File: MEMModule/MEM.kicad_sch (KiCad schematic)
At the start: 5 parts, among them U1 74ABT32, U2 74AHCT04

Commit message: MEMModule now has ROM on Bank 0 again
The idea of having a system with no built-in ROM is turning out to be more
complicated than I expected. The boot device is additional complexity that
I'm now reluctant to take on. It's still, after months, not fully designed
and prototyped. Let's eliminate the need for this entire module by having
the computer run from ROM on boot.

The benefits of a ROM-less system are more difficult to achieve than
expected. The device would need a fast sixteen bit ALU chip as in the
program counter. Using simple counters like the 74F161 would bottleneck the
counting sopeed at 12.5MHz and the boot device provides no effective speed
benefit.

Further, the entire scheme is a performance optimization for a machine that
hasn't even been fully constructed yet. I can take on optimization work
later.

So this change sticks a pair of fast ROMS into MEM on Bank zero. A program
can set the Bank register to something else in order to map the built-in
RAM to instruction memory instead.

Also, update MEMModule for KiCad 7.
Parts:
- removed unit 4 of U2
- removed unit 3 of U2
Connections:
- no-connect marks 6 -> 4

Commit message: Update part info and data sheet links, move onto the 1.27mm grid
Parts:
- C2, C3: value 100nF -> 0.1μF
- U2: Mouser https://www.mouser.com/ProductDetail/771-AHCT04PW112 -> https://www.mouser.com/ProductDetail/Nexperia/74AHCT04APWJ?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

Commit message: MEMModule: Fix bug in the bank register reset signal
The bank register expects an active-high reset signal but was wired to
receive an active-low signal. Fix this issue by routing /RST_sync through
an inverter first.

BUG: The MainBoard PCB layout has not been updated yet.
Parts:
- removed unit 5 of U2
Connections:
- no-connect marks 4 -> 3
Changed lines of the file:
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@@
   (junction (at -44.45 146.05) (diameter 0) (color 0 0 0 0)
-  )
-  (junction (at -21.59 133.35) (diameter 0) (color 0 0 0 0)
   )
   (junction (at -44.45 130.81) (diameter 0) (color 0 0 0 0)
@@
   (no_connect (at -6.35 146.05))
   (no_connect (at -26.67 128.27))
-  (no_connect (at -6.35 133.35))
   (no_connect (at -26.67 143.51))
   (bus_entry (at 58.42 58.42) (size 2.54 2.54)
@@
     (stroke (width 0) (type default))
   )
-  (wire (pts (xy -21.59 97.79) (xy -21.59 133.35))
+  (wire (pts (xy -21.59 97.79) (xy -21.59 146.05))
     (stroke (width 0) (type default))
   )
@@
   )
   (wire (pts (xy 83.82 121.92) (xy 91.44 121.92))
-    (stroke (width 0) (type default))
-  )
-  (wire (pts (xy -21.59 133.35) (xy -21.59 146.05))
     (stroke (width 0) (type default))
   )
@@
         )
       )
-    )
-  )
-  (symbol (lib_id "74xx:74LS04") (at -13.97 133.35 0) (unit 5)
-    (in_bom yes) (on_board yes) (dnp no)
-    (property "Reference" "U2" (at -13.97 125.2982 0)
-      (effects (font (size 1.27 1.27)))
-    )
-    (property "Value" "74AHCT04" (at -13.97 127.6096 0)
-      (effects (font (size 1.27 1.27)))
-    )
-    (property "Footprint" "Package_SO:TSSOP-14_4.4x5mm_P0.65mm" (at -13.97 133.35 0)
-      (effects (font (size 1.27 1.27)) hide)
-    )
-    (property "Datasheet" "https://www.mouser.com/datasheet/2/916/74AHCT04A-1545508.pdf" (at -13.97 133.35 0)
-      (effects (font (size 1.27 1.27)) hide)
-    )
-    (property "Mouser" "https://www.mouser.com/ProductDetail/Nexperia/74AHCT04APWJ?qs=5aG0NVq1C4yf8jbQquj09Q==" (at -13.97 133.35 0)
-      (effects (font (size 1.27 1.27)) hide)
-    )
-    (pin "1")
-    (pin "2")
-    (pin "3")
-    (pin "4")
-    (pin "5")
-    (pin "6")
-    (pin "8")
-    (pin "9")
-    (pin "10")
-    (pin "11")
-    (pin "12")
-    (pin "13")
-    (pin "14")
-    (pin "7")
-    (instances
-      (project "MEMModule"
-        (path "/83c5181e-f5ee-453c-ae5c-d7256ba8837d/00000000-0000-0000-0000-000060af64de"
-          (reference "U2") (unit 5)
-        )
-      )

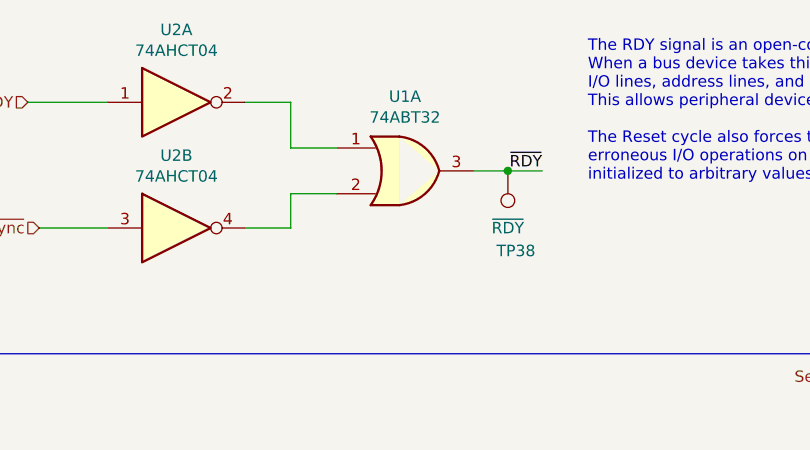
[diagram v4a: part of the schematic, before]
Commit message: MEMModule: incorporate fix to the bank register in Rev D
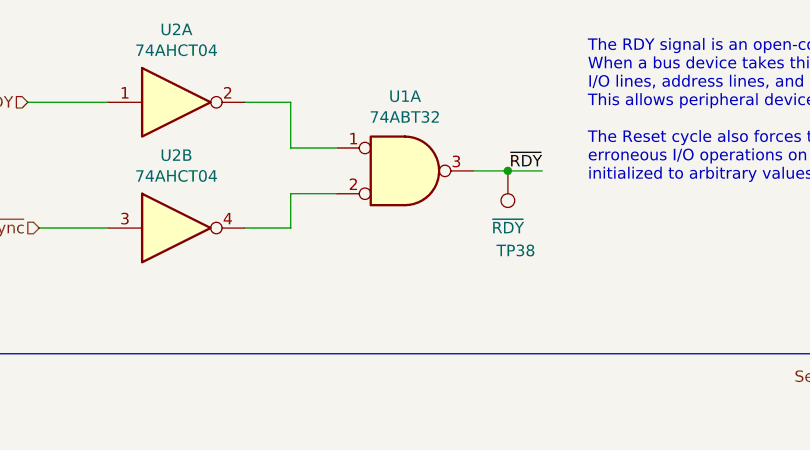
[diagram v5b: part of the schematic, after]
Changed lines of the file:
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@@
   (title_block
     (title "MEM")
-    (date "2023-03-22")
-    (rev "B")
+    (date "2023-10-28")
+    (rev "D")
     (comment 1 "place bus lines into tristate and halt the Phi1 clock.")
     (comment 2 "Devices on the bus may take the open-collector ~RDY~ signal high to force the CPU to")
@@
     )
   )
-  (symbol (lib_id "74xx:74LS32") (at 113.03 38.1 0) (unit 1)
+  (symbol (lib_id "74xx:74LS32") (at 113.03 38.1 0) (unit 1) (convert 2)
     (in_bom yes) (on_board yes) (dnp no)
     (property "Reference" "U1" (at 113.03 29.845 0)

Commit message: MEMModule: Add jumper for single-step mode
This works around an issue where MEM never asserts signals to the bus in
single-step mode. Now, we can set the jumper to force MEM to assert these
signals as-if the computer is ready, even when it's not.
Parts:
- added J4: Single Step, Connector_PinHeader_2.54mm:PinHeader_1x03_P2.54mm_Vertical, symbol Connector:Conn_01x03_Pin
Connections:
- net GND: now also J4.3 (Pin_3)
- net RDY: now also U1.10; no longer U2.1
- net VCC: now also J4.1 (Pin_1); no longer U1.10, U1.9
- net at U1.8: now also U2.1
- new net: J4.2 (Pin_2), U1.9
- no-connect marks 3 -> 2
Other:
- note added: "Set the Single Step jumper during operation in single-step mode. In this mode, the RDY signal is low on every clock tick, and MEM would otherwise not ever assert signals the bus."
- moved on the sheet: U1C
